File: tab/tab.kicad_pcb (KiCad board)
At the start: 2 copper layers, 29 x 19 mm, 14 parts

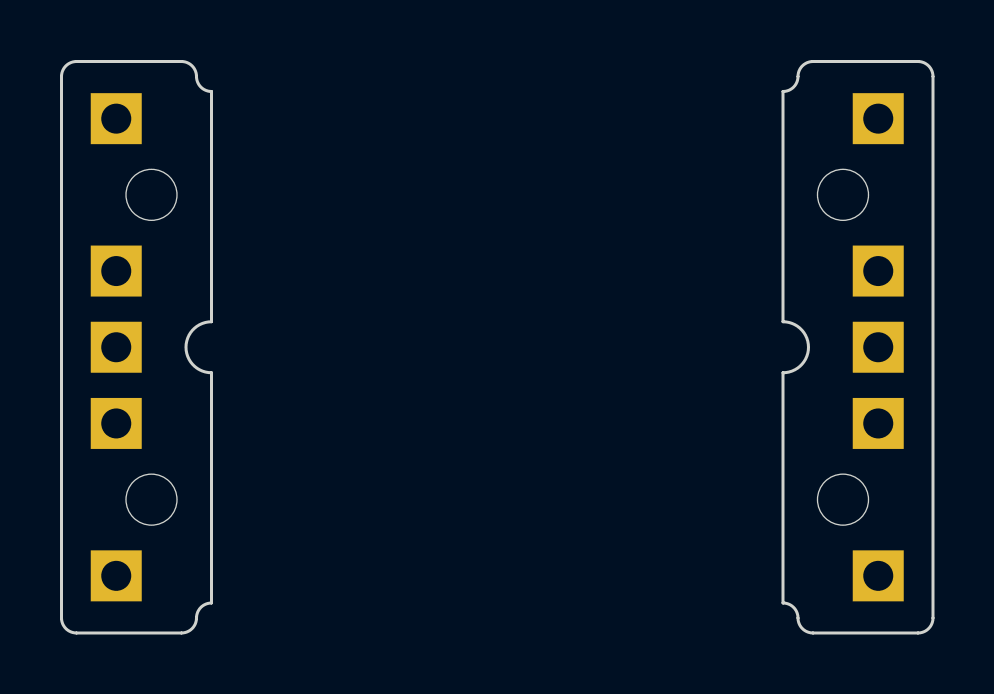
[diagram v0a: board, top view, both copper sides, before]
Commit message: fixes left and right tabs
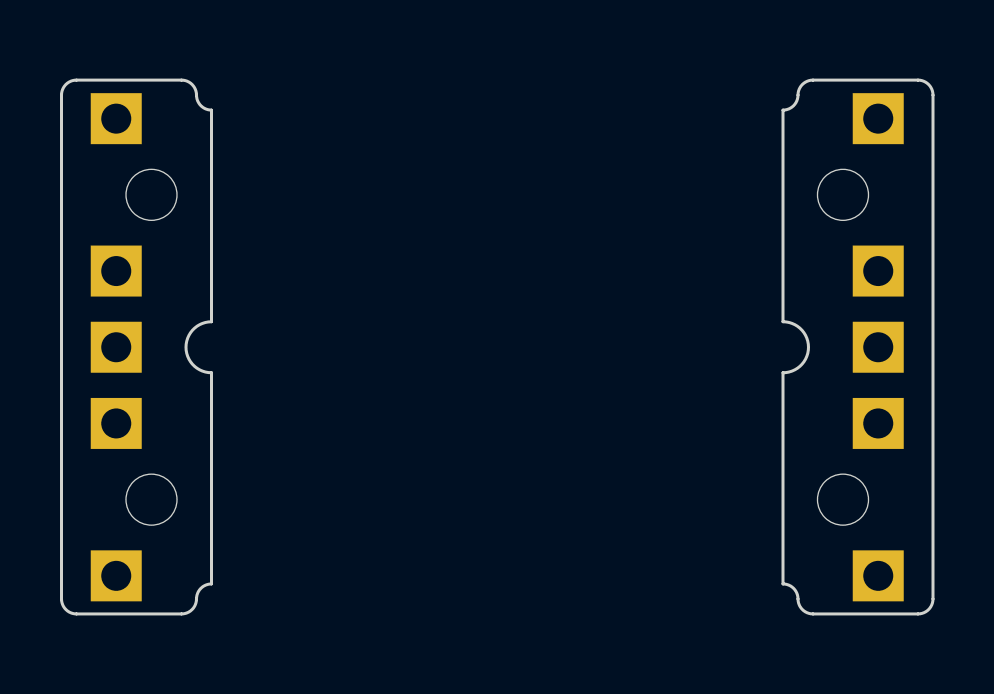
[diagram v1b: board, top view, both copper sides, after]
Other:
- board size 29 x 19 mm -> 29 x 17.8 mm
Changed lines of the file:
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@@
     (pad "1" thru_hole rect (at 0 0 180) (size 1.7 1.7) (drill 1) (layers "*.Cu" "*.Mask"))
   )
-  (gr_arc (start 83.455 69.215) (mid 83.808553 69.361447) (end 83.955 69.715)
+  (gr_arc (start 83.455 69.835) (mid 83.808553 69.981447) (end 83.955 70.335)
     (stroke (width 0.1) (type default)) (layer "Edge.Cuts"))
-  (gr_line (start 83.455 69.215) (end 79.955 69.215)
+  (gr_line (start 83.455 69.835) (end 79.955 69.835)
     (stroke (width 0.1) (type default)) (layer "Edge.Cuts"))
-  (gr_arc (start 84.455 70.215) (mid 84.101447 70.068553) (end 83.955 69.715)
+  (gr_arc (start 84.455 70.835) (mid 84.101447 70.688553) (end 83.955 70.335)
     (stroke (width 0.1) (type default)) (layer "Edge.Cuts"))
-  (gr_arc (start 104.005 69.715) (mid 104.151447 69.361447) (end 104.505 69.215)
+  (gr_arc (start 104.005 70.335) (mid 104.151447 69.981447) (end 104.505 69.835)
     (stroke (width 0.1) (type default)) (layer "Edge.Cuts"))
-  (gr_line (start 103.505 77.89) (end 103.505 70.215)
+  (gr_line (start 103.505 77.89) (end 103.505 70.835)
     (stroke (width 0.1) (type default)) (layer "Edge.Cuts"))
-  (gr_arc (start 79.455 69.715) (mid 79.601447 69.361447) (end 79.955 69.215)
+  (gr_arc (start 79.455 70.335) (mid 79.601447 69.981447) (end 79.955 69.835)
     (stroke (width 0.1) (type default)) (layer "Edge.Cuts"))
-  (gr_arc (start 83.955 87.765) (mid 83.808553 88.118553) (end 83.455 88.265)
+  (gr_arc (start 83.955 87.13) (mid 83.808553 87.483553) (end 83.455 87.63)
     (stroke (width 0.1) (type default)) (layer "Edge.Cuts"))
-  (gr_line (start 84.455 70.215) (end 84.455 77.89)
+  (gr_line (start 84.455 70.835) (end 84.455 77.89)
     (stroke (width 0.1) (type default)) (layer "Edge.Cuts"))
   (gr_arc (start 103.505 77.89) (mid 104.355 78.74) (end 103.505 79.59)
     (stroke (width 0.1) (type default)) (layer "Edge.Cuts"))
-  (gr_line (start 103.505 87.265) (end 103.505 79.59)
+  (gr_line (start 103.505 86.63) (end 103.505 79.59)
     (stroke (width 0.1) (type default)) (layer "Edge.Cuts"))
-  (gr_line (start 84.455 79.59) (end 84.455 87.265)
+  (gr_line (start 84.455 79.59) (end 84.455 86.63)
     (stroke (width 0.1) (type default)) (layer "Edge.Cuts"))
-  (gr_line (start 104.505 69.215) (end 108.005 69.215)
+  (gr_line (start 104.505 69.835) (end 108.005 69.835)
     (stroke (width 0.1) (type default)) (layer "Edge.Cuts"))
-  (gr_arc (start 79.955 88.265) (mid 79.601447 88.118553) (end 79.455 87.765)
+  (gr_arc (start 79.955 87.63) (mid 79.601447 87.483553) (end 79.455 87.13)
     (stroke (width 0.1) (type default)) (layer "Edge.Cuts"))
-  (gr_line (start 104.505 88.265) (end 108.005 88.265)
+  (gr_line (start 104.505 87.63) (end 108.005 87.63)
     (stroke (width 0.1) (type default)) (layer "Edge.Cuts"))
   (gr_arc (start 84.455 79.59) (mid 83.605 78.74) (end 84.455 77.89)
     (stroke (width 0.1) (type default)) (layer "Edge.Cuts"))
-  (gr_line (start 83.455 88.265) (end 79.955 88.265)
+  (gr_line (start 83.455 87.63) (end 79.955 87.63)
     (stroke (width 0.1) (type default)) (layer "Edge.Cuts"))
-  (gr_line (start 79.455 87.765) (end 79.455 69.715)
+  (gr_line (start 79.455 87.13) (end 79.455 70.335)
     (stroke (width 0.1) (type default)) (layer "Edge.Cuts"))
-  (gr_arc (start 104.005 69.715) (mid 103.858553 70.068553) (end 103.505 70.215)
+  (gr_arc (start 104.005 70.335) (mid 103.858553 70.688553) (end 103.505 70.835)
     (stroke (width 0.1) (type default)) (layer "Edge.Cuts"))
-  (gr_arc (start 108.505 87.765) (mid 108.358553 88.118553) (end 108.005 88.265)
+  (gr_arc (start 108.505 87.13) (mid 108.358553 87.483553) (end 108.005 87.63)
     (stroke (width 0.1) (type default)) (layer "Edge.Cuts"))
-  (gr_line (start 108.505 69.715) (end 108.505 87.765)
+  (gr_line (start 108.505 70.335) (end 108.505 87.13)
     (stroke (width 0.1) (type default)) (layer "Edge.Cuts"))
-  (gr_arc (start 83.955 87.765) (mid 84.101447 87.411447) (end 84.455 87.265)
+  (gr_arc (start 83.955 87.13) (mid 84.101447 86.776447) (end 84.455 86.63)
     (stroke (width 0.1) (type default)) (layer "Edge.Cuts"))
-  (gr_arc (start 108.005 69.215) (mid 108.358553 69.361447) (end 108.505 69.715)
+  (gr_arc (start 108.005 69.835) (mid 108.358553 69.981447) (end 108.505 70.335)
     (stroke (width 0.1) (type default)) (layer "Edge.Cuts"))
-  (gr_arc (start 103.505 87.265) (mid 103.858553 87.411447) (end 104.005 87.765)
+  (gr_arc (start 103.505 86.63) (mid 103.858553 86.776447) (end 104.005 87.13)
     (stroke (width 0.1) (type default)) (layer "Edge.Cuts"))
-  (gr_arc (start 104.505 88.265) (mid 104.151447 88.118553) (end 104.005 87.765)
+  (gr_arc (start 104.505 87.63) (mid 104.151447 87.483553) (end 104.005 87.13)
     (stroke (width 0.1) (type default)) (layer "Edge.Cuts"))
   (gr_text "Short     R1&2\n to share GND" (at 105.94 74.465 90) (layer "B.SilkS")

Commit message: make symmetric
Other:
- outline, holes or cut-outs redrawn
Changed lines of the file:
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@@
     (pad "1" thru_hole rect (at 0 0 180) (size 1.7 1.7) (drill 1) (layers "*.Cu" "*.Mask"))
   )
-  (gr_arc (start 83.455 69.835) (mid 83.808553 69.981447) (end 83.955 70.335)
+  (gr_arc (start 83.455 69.85) (mid 83.808553 69.996447) (end 83.955 70.35)
     (stroke (width 0.1) (type default)) (layer "Edge.Cuts"))
-  (gr_line (start 83.455 69.835) (end 79.955 69.835)
+  (gr_line (start 83.455 69.85) (end 79.955 69.85)
     (stroke (width 0.1) (type default)) (layer "Edge.Cuts"))
-  (gr_arc (start 84.455 70.835) (mid 84.101447 70.688553) (end 83.955 70.335)
+  (gr_arc (start 84.455 70.85) (mid 84.101447 70.703553) (end 83.955 70.35)
     (stroke (width 0.1) (type default)) (layer "Edge.Cuts"))
-  (gr_arc (start 104.005 70.335) (mid 104.151447 69.981447) (end 104.505 69.835)
+  (gr_line (start 108.005 69.85) (end 104.505 69.85)
     (stroke (width 0.1) (type default)) (layer "Edge.Cuts"))
-  (gr_line (start 103.505 77.89) (end 103.505 70.835)
+  (gr_arc (start 104.005 70.35) (mid 104.151447 69.996447) (end 104.505 69.85)
     (stroke (width 0.1) (type default)) (layer "Edge.Cuts"))
-  (gr_arc (start 79.455 70.335) (mid 79.601447 69.981447) (end 79.955 69.835)
+  (gr_line (start 103.505 77.89) (end 103.505 70.85)
+    (stroke (width 0.1) (type default)) (layer "Edge.Cuts"))
+  (gr_arc (start 79.455 70.35) (mid 79.601447 69.996447) (end 79.955 69.85)
     (stroke (width 0.1) (type default)) (layer "Edge.Cuts"))
   (gr_arc (start 83.955 87.13) (mid 83.808553 87.483553) (end 83.455 87.63)
     (stroke (width 0.1) (type default)) (layer "Edge.Cuts"))
-  (gr_line (start 84.455 70.835) (end 84.455 77.89)
+  (gr_line (start 84.455 70.85) (end 84.455 77.89)
     (stroke (width 0.1) (type default)) (layer "Edge.Cuts"))
   (gr_arc (start 103.505 77.89) (mid 104.355 78.74) (end 103.505 79.59)
@@
     (stroke (width 0.1) (type default)) (layer "Edge.Cuts"))
   (gr_line (start 84.455 79.59) (end 84.455 86.63)
-    (stroke (width 0.1) (type default)) (layer "Edge.Cuts"))
-  (gr_line (start 104.505 69.835) (end 108.005 69.835)
     (stroke (width 0.1) (type default)) (layer "Edge.Cuts"))
   (gr_arc (start 79.955 87.63) (mid 79.601447 87.483553) (end 79.455 87.13)
@@
   (gr_line (start 83.455 87.63) (end 79.955 87.63)
     (stroke (width 0.1) (type default)) (layer "Edge.Cuts"))
-  (gr_line (start 79.455 87.13) (end 79.455 70.335)
+  (gr_line (start 79.455 87.13) (end 79.455 70.35)
     (stroke (width 0.1) (type default)) (layer "Edge.Cuts"))
-  (gr_arc (start 104.005 70.335) (mid 103.858553 70.688553) (end 103.505 70.835)
+  (gr_arc (start 104.005 70.35) (mid 103.858553 70.703553) (end 103.505 70.85)
     (stroke (width 0.1) (type default)) (layer "Edge.Cuts"))
   (gr_arc (start 108.505 87.13) (mid 108.358553 87.483553) (end 108.005 87.63)
     (stroke (width 0.1) (type default)) (layer "Edge.Cuts"))
-  (gr_line (start 108.505 70.335) (end 108.505 87.13)
+  (gr_line (start 108.505 70.35) (end 108.505 87.13)
     (stroke (width 0.1) (type default)) (layer "Edge.Cuts"))
   (gr_arc (start 83.955 87.13) (mid 84.101447 86.776447) (end 84.455 86.63)
     (stroke (width 0.1) (type default)) (layer "Edge.Cuts"))
-  (gr_arc (start 108.005 69.835) (mid 108.358553 69.981447) (end 108.505 70.335)
+  (gr_arc (start 108.005 69.85) (mid 108.358553 69.996447) (end 108.505 70.35)
     (stroke (width 0.1) (type default)) (layer "Edge.Cuts"))
   (gr_arc (start 103.505 86.63) (mid 103.858553 86.776447) (end 104.005 87.13)
